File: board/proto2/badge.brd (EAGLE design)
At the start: 136.5 x 119 mm, 59 parts, among them IC1 TLV62569, J1 5051101092

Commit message: reduce LEDs to 14, add tilt switch, draw NFC antenna
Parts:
- removed C19, C23: .1u, rcl:C0201
- removed LED15, LED16: WS2812B, badge:WS2812B
- added S7: SW-200D, badge:SW-200D
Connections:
- removed net N$26: LED15.2, LED16.4
- net +3V3: no longer C19.1, C23.1, LED15.1, LED16.1
- net GND: now also S7.1; no longer C19.2, C23.2, LED15.3, LED16.3
- net N$21: now also S7.2, U1.P37; no longer LED14.2, LED15.4
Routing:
- net ANT: track 0.00 -> 405.1 mm

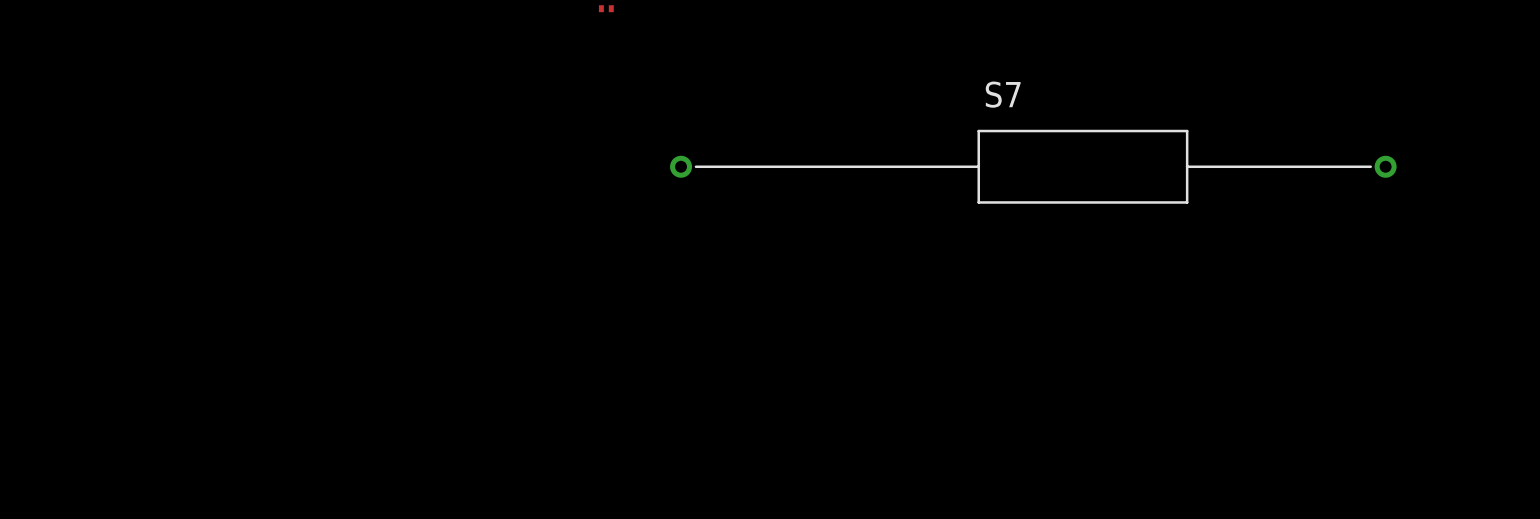
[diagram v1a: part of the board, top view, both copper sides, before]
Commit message: added SD card holder to schematic
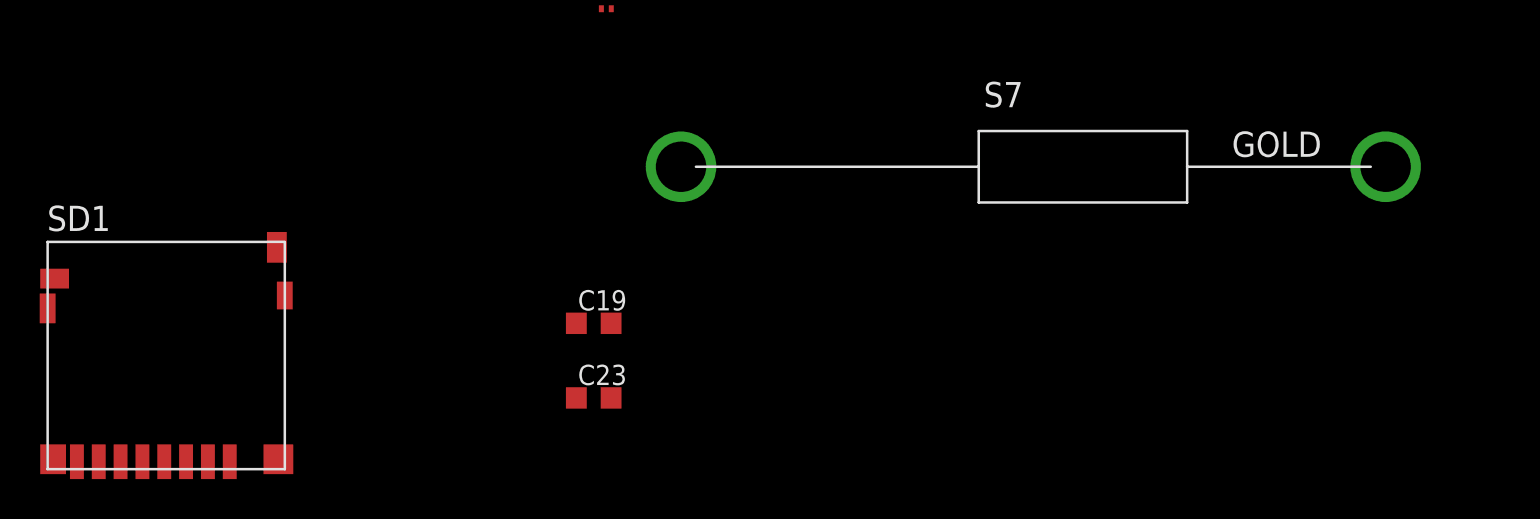
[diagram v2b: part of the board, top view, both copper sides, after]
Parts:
- added C19, C23: 300p, rcl:C0603K
- added SD1: 114-00841-68, badge:114-00841-68
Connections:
- new net ANT: C19.1, C23.1, U1.P25, U1.P26
- new net P0.03: SD1.SWA, U1.P19
- new net P0.04: SD1.7, U1.P20
- new net P0.05: SD1.5, U1.P21
- new net P0.06: SD1.3, U1.P22
- new net P0.07: SD1.2, U1.P23
- net +3V3: now also SD1.4
- net GND: now also C19.2, C23.2, S7.A, SD1.6, SD1.G1, SD1.G2, SD1.G3, SD1.G4, SD1.SWB; no longer S7.1
- net N$21: now also S7.C; no longer S7.2
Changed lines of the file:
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@@
 <layer number="20" name="Dimension" color="15" fill="1" visible="yes" active="yes"/>
 <layer number="21" name="tPlace" color="7" fill="1" visible="yes" active="yes"/>
-<layer number="22" name="bPlace" color="7" fill="1" visible="yes" active="yes"/>
+<layer number="22" name="bPlace" color="7" fill="1" visible="no" active="yes"/>
 <layer number="23" name="tOrigins" color="15" fill="1" visible="yes" active="yes"/>
-<layer number="24" name="bOrigins" color="15" fill="1" visible="yes" active="yes"/>
-<layer number="25" name="tNames" color="7" fill="1" visible="no" active="yes"/>
+<layer number="24" name="bOrigins" color="15" fill="1" visible="no" active="yes"/>
+<layer number="25" name="tNames" color="7" fill="1" visible="yes" active="yes"/>
 <layer number="26" name="bNames" color="7" fill="1" visible="no" active="yes"/>
 <layer number="27" name="tValues" color="7" fill="1" visible="no" active="yes"/>
@@
 <element name="C22" library="rcl" package="C0201" value=".1u" x="-59.69" y="-445.77"/>
 <element name="S7" library="badge" package="SW-200D" value="SW-200D" x="-35.676" y="-453.732"/>
+<element name="C19" library="rcl" package="C0603K" value="300p" x="-60.325" y="-461.6196"/>
+<element name="C23" library="rcl" package="C0603K" value="300p" x="-60.325" y="-465.3788"/>
+<element name="SD1" library="badge" package="114-00841-68" value="114-00841-68" x="-81.8642" y="-469.4682"/>
 </elements>
 <signals>
@@
 <contactref element="C21" pad="2"/>
 <contactref element="C22" pad="2"/>
-<contactref element="S7" pad="1"/>
+<contactref element="S7" pad="A"/>
+<contactref element="C23" pad="2"/>
+<contactref element="C19" pad="2"/>
+<contactref element="SD1" pad="G2"/>
+<contactref element="SD1" pad="G3"/>
+<contactref element="SD1" pad="G1"/>
+<contactref element="SD1" pad="G4"/>
+<contactref element="SD1" pad="6"/>
+<contactref element="SD1" pad="SWB"/>
 <wire x1="-59.44" y1="-440.69" x2="-59.44" y2="-445.77" width="0" layer="19" extent="1-1"/>
 <wire x1="-59.44" y1="-435.61" x2="-59.44" y2="-440.69" width="0" layer="19" extent="1-1"/>
@@
 <wire x1="-59.44" y1="-389.89" x2="-59.44" y2="-394.97" width="0" layer="19" extent="1-1"/>
 <wire x1="-55.926" y1="-453.732" x2="-59.44" y2="-445.77" width="0" layer="19" extent="1-1"/>
+<wire x1="-59.45" y1="-461.6196" x2="-55.926" y2="-453.732" width="0" layer="19" extent="1-1"/>
+<wire x1="-59.45" y1="-465.3788" x2="-59.45" y2="-461.6196" width="0" layer="19" extent="1-1"/>
+<wire x1="-75.8892" y1="-460.2182" x2="-59.45" y2="-461.6196" width="0" layer="19" extent="1-1"/>
+<wire x1="-76.2892" y1="-457.7932" x2="-75.8892" y2="-460.2182" width="0" layer="19" extent="1-1"/>
+<wire x1="-76.2142" y1="-468.4682" x2="-75.8892" y2="-460.2182" width="0" layer="19" extent="1-1"/>
+<wire x1="-84.1642" y1="-468.5932" x2="-76.2142" y2="-468.4682" width="0" layer="19" extent="1-1"/>
+<wire x1="-87.5642" y1="-468.4682" x2="-84.1642" y2="-468.5932" width="0" layer="19" extent="1-1"/>
+<wire x1="-87.8392" y1="-460.8682" x2="-87.5642" y2="-468.4682" width="0" layer="19" extent="1-1"/>
 <wire x1="-57.89" y1="-232.57" x2="-59.44" y2="-389.89" width="0" layer="19" extent="1-1"/>
 <wire x1="-53.09" y1="-229.87" x2="-57.89" y2="-232.57" width="0" layer="19" extent="1-1"/>
@@
 <contactref element="C21" pad="1"/>
 <contactref element="C22" pad="1"/>
+<contactref element="SD1" pad="4"/>
 <wire x1="-55.75" y1="-182.88" x2="-58.84" y2="-191.77" width="0" layer="19" extent="1-1"/>
 <wire x1="-51.8" y1="-185.42" x2="-55.75" y2="-182.88" width="0" layer="19" extent="1-1"/>
@@
 <wire x1="-54.86" y1="-440.69" x2="-59.94" y2="-440.69" width="0" layer="19" extent="1-1"/>
 <wire x1="-54.86" y1="-430.53" x2="-59.94" y2="-430.53" width="0" layer="19" extent="1-1"/>
+<wire x1="-81.9642" y1="-468.5932" x2="-59.94" y2="-445.77" width="0" layer="19" extent="1-1"/>
 <wire x1="56.508846875" y1="21.687634375" x2="-55.75" y2="-182.88" width="0" layer="19" extent="1-1"/>
 <wire x1="51.739375" y1="45.459525" x2="56.508846875" y2="21.687634375" width="0" layer="19" extent="1-1"/>
@@
 </signal>
 <signal name="N$21">
-<contactref element="S7" pad="2"/>
+<contactref element="S7" pad="C"/>
 <contactref element="U1" pad="P37"/>
 <wire x1="70.688115625" y1="92.58431875" x2="-20.426" y2="-453.732" width="0" layer="19" extent="1-1"/>
@@
 <wire x1="85.4202" y1="-43.4594" x2="68.7578" y2="-43.4594" width="0.5334" layer="16"/>
 <wire x1="68.7578" y1="-43.4594" x2="68.7578" y2="-28.8798" width="0.5334" layer="16"/>
+<contactref element="U1" pad="P26"/>
+<contactref element="U1" pad="P25"/>
+<contactref element="C23" pad="1"/>
+<contactref element="C19" pad="1"/>
+<wire x1="67.388115625" y1="88.18431875" x2="67.938115625" y2="89.08431875" width="0" layer="19" extent="1-1"/>
+<wire x1="64.5922" y1="-23.6728" x2="67.388115625" y2="88.18431875" width="0" layer="19" extent="1-16"/>
+<wire x1="-61.2" y1="-461.6196" x2="64.5922" y2="-47.625" width="0" layer="19" extent="1-16"/>
+<wire x1="-61.2" y1="-465.3788" x2="-61.2" y2="-461.6196" width="0" layer="19" extent="1-1"/>
+</signal>
+<signal name="P0.04">
+<contactref element="SD1" pad="7"/>
+<contactref element="U1" pad="P20"/>
+<wire x1="-85.2642" y1="-468.5932" x2="64.638115625" y2="89.08431875" width="0" layer="19" extent="1-1"/>
+</signal>
+<signal name="P0.07">
+<contactref element="SD1" pad="2"/>
+<contactref element="U1" pad="P23"/>
+<wire x1="-79.7642" y1="-468.5932" x2="66.288115625" y2="88.18431875" width="0" layer="19" extent="1-1"/>
+</signal>
+<signal name="P0.06">
+<contactref element="SD1" pad="3"/>
+<contactref element="U1" pad="P22"/>
+<wire x1="-80.8642" y1="-468.5932" x2="65.738115625" y2="89.08431875" width="0" layer="19" extent="1-1"/>
+</signal>
+<signal name="P0.05">
+<contactref element="SD1" pad="5"/>
+<contactref element="U1" pad="P21"/>
+<wire x1="-83.0642" y1="-468.5932" x2="65.188115625" y2="88.18431875" width="0" layer="19" extent="1-1"/>
+</signal>
+<signal name="P0.03">
+<contactref element="SD1" pad="SWA"/>
+<contactref element="U1" pad="P19"/>
+<wire x1="-87.4892" y1="-459.3682" x2="64.088115625" y2="88.18431875" width="0" layer="19" extent="1-1"/>
 </signal>
 </signals>

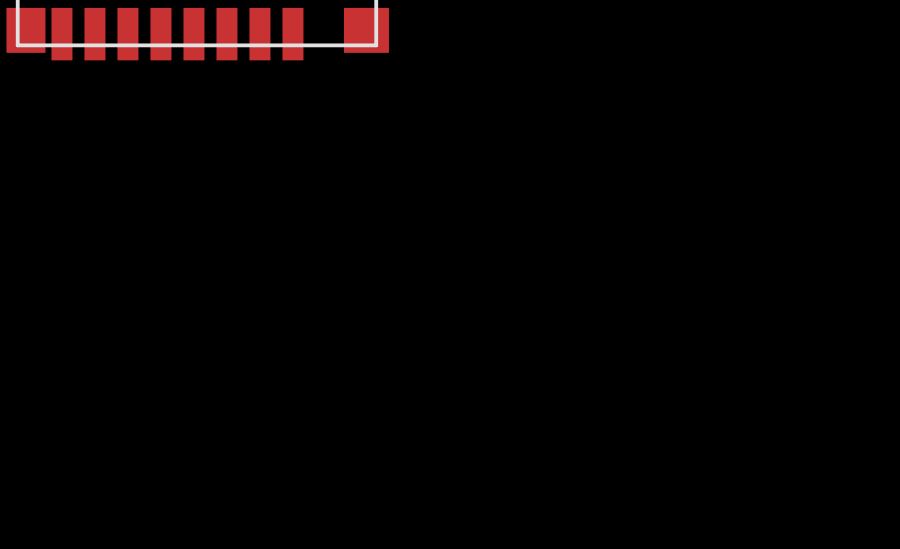
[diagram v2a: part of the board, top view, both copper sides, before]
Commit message: added expansion connector to schematic
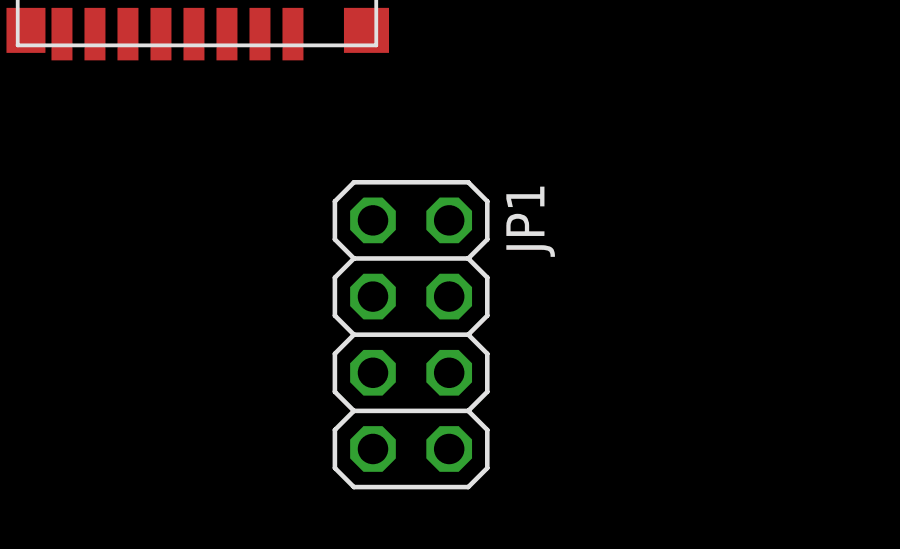
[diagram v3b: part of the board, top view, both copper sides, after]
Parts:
- added JP1: (no value), pinhead:2X04
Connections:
- new net P0.00: JP1.4, U1.P13
- new net P0.01: JP1.6, U1.P14
- new net P0.29: JP1.7, U1.P10
- new net P0.30: JP1.5, U1.P11
- new net P0.31: JP1.3, U1.P12
- net +3V3: now also JP1.1
- net GND: now also JP1.2, JP1.8
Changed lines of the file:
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@@
 <setting verticaltext="up"/>
 </settings>
-<grid distance="1" unitdist="mil" unit="mm" style="lines" multiple="1" display="yes" altdistance="0.012" altunitdist="mm" altunit="mm"/>
+<grid distance="1" unitdist="mil" unit="inch" style="lines" multiple="1" display="yes" altdistance="0.012" altunitdist="mm" altunit="mm"/>
 <layers>
 <layer number="1" name="Top" color="4" fill="1" visible="yes" active="yes"/>
@@
 <element name="C23" library="rcl" package="C0603K" value="300p" x="-60.325" y="-465.3788"/>
 <element name="SD1" library="badge" package="114-00841-68" value="114-00841-68" x="-81.8642" y="-469.4682"/>
+<element name="JP1" library="pinhead" package="2X04" value="" x="-74.7268" y="-478.6122" rot="R270"/>
 </elements>
 <signals>
@@
 <contactref element="SD1" pad="6"/>
 <contactref element="SD1" pad="SWB"/>
+<contactref element="JP1" pad="2"/>
+<contactref element="JP1" pad="8"/>
 <wire x1="-59.44" y1="-440.69" x2="-59.44" y2="-445.77" width="0" layer="19" extent="1-1"/>
 <wire x1="-59.44" y1="-435.61" x2="-59.44" y2="-440.69" width="0" layer="19" extent="1-1"/>
@@
 <wire x1="-76.2892" y1="-457.7932" x2="-75.8892" y2="-460.2182" width="0" layer="19" extent="1-1"/>
 <wire x1="-76.2142" y1="-468.4682" x2="-75.8892" y2="-460.2182" width="0" layer="19" extent="1-1"/>
+<wire x1="-73.4568" y1="-474.8022" x2="-76.2142" y2="-468.4682" width="0" layer="19" extent="1-1"/>
+<wire x1="-73.4568" y1="-482.4222" x2="-73.4568" y2="-474.8022" width="0" layer="19" extent="1-1"/>
 <wire x1="-84.1642" y1="-468.5932" x2="-76.2142" y2="-468.4682" width="0" layer="19" extent="1-1"/>
 <wire x1="-87.5642" y1="-468.4682" x2="-84.1642" y2="-468.5932" width="0" layer="19" extent="1-1"/>
@@
 <contactref element="C22" pad="1"/>
 <contactref element="SD1" pad="4"/>
+<contactref element="JP1" pad="1"/>
 <wire x1="-55.75" y1="-182.88" x2="-58.84" y2="-191.77" width="0" layer="19" extent="1-1"/>
 <wire x1="-51.8" y1="-185.42" x2="-55.75" y2="-182.88" width="0" layer="19" extent="1-1"/>
@@
 <wire x1="-54.86" y1="-430.53" x2="-59.94" y2="-430.53" width="0" layer="19" extent="1-1"/>
 <wire x1="-81.9642" y1="-468.5932" x2="-59.94" y2="-445.77" width="0" layer="19" extent="1-1"/>
+<wire x1="-75.9968" y1="-474.8022" x2="-81.9642" y2="-468.5932" width="0" layer="19" extent="1-1"/>
 <wire x1="56.508846875" y1="21.687634375" x2="-55.75" y2="-182.88" width="0" layer="19" extent="1-1"/>
 <wire x1="51.739375" y1="45.459525" x2="56.508846875" y2="21.687634375" width="0" layer="19" extent="1-1"/>
@@
 <wire x1="-87.4892" y1="-459.3682" x2="64.088115625" y2="88.18431875" width="0" layer="19" extent="1-1"/>
 </signal>
+<signal name="P0.31">
+<contactref element="JP1" pad="3"/>
+<contactref element="U1" pad="P12"/>
+<wire x1="-75.9968" y1="-477.3422" x2="62.788115625" y2="90.93431875" width="0" layer="19" extent="1-1"/>
+</signal>
+<signal name="P0.30">
+<contactref element="JP1" pad="5"/>
+<contactref element="U1" pad="P11"/>
+<wire x1="-75.9968" y1="-479.8822" x2="61.888115625" y2="91.48431875" width="0" layer="19" extent="1-1"/>
+</signal>
+<signal name="P0.29">
+<contactref element="JP1" pad="7"/>
+<contactref element="U1" pad="P10"/>
+<wire x1="-75.9968" y1="-482.4222" x2="62.788115625" y2="92.03431875" width="0" layer="19" extent="1-1"/>
+</signal>
+<signal name="P0.00">
+<contactref element="JP1" pad="4"/>
+<contactref element="U1" pad="P13"/>
+<wire x1="-73.4568" y1="-477.3422" x2="61.888115625" y2="90.38431875" width="0" layer="19" extent="1-1"/>
+</signal>
+<signal name="P0.01">
+<contactref element="JP1" pad="6"/>
+<contactref element="U1" pad="P14"/>
+<wire x1="-73.4568" y1="-479.8822" x2="62.788115625" y2="89.83431875" width="0" layer="19" extent="1-1"/>
+</signal>
 </signals>

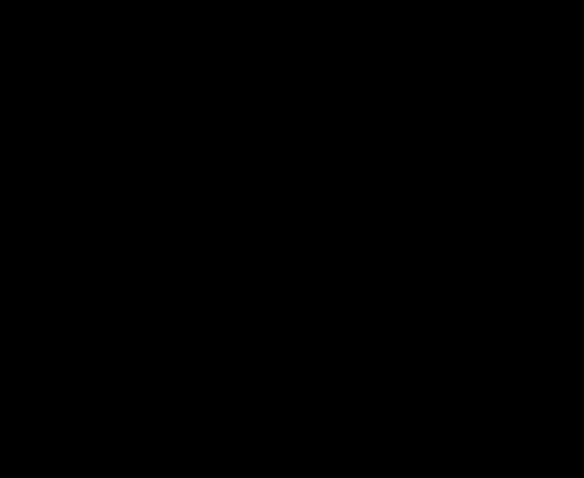
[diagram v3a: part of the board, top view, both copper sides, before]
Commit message: added programming cable connector
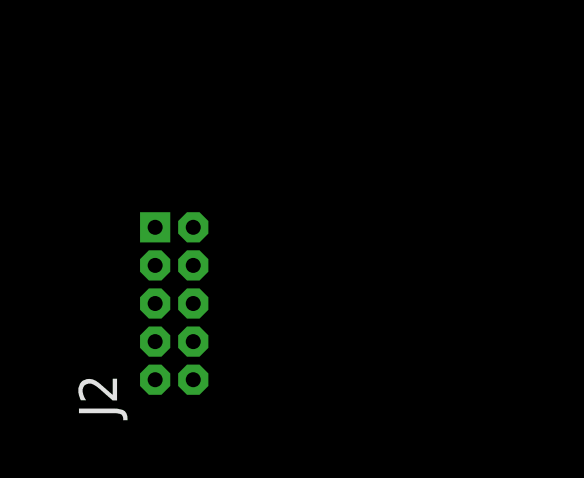
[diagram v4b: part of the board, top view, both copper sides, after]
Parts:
- added J2: M05X2X1.27, badge:2X5X1.27
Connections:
- removed net N$11: C6.1, IC1.1, IC1.4, S6.2
- new net N$26: J2.2, U1.P44
- new net N$31: J2.4, U1.P43
- new net N$32: J2.6, U1.P36
- new net N$33: J2.10, U1.P39
- new net VBAT: C6.1, IC1.1, IC1.4, J2.7, S6.2
- net +3V3: now also J2.1
- net GND: now also J2.3, J2.5
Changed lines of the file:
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@@
 <element name="SD1" library="badge" package="114-00841-68" value="114-00841-68" x="-81.8642" y="-469.4682"/>
 <element name="JP1" library="pinhead" package="2X04" value="" x="-74.7268" y="-478.6122" rot="R270"/>
+<element name="J2" library="badge" package="2X5X1.27" value="M05X2X1.27" x="-96.2406" y="-479.9076"/>
 </elements>
 <signals>
@@
 <contactref element="JP1" pad="2"/>
 <contactref element="JP1" pad="8"/>
+<contactref element="J2" pad="3"/>
+<contactref element="J2" pad="5"/>
 <wire x1="-59.44" y1="-440.69" x2="-59.44" y2="-445.77" width="0" layer="19" extent="1-1"/>
 <wire x1="-59.44" y1="-435.61" x2="-59.44" y2="-440.69" width="0" layer="19" extent="1-1"/>
@@
 <wire x1="-87.5642" y1="-468.4682" x2="-84.1642" y2="-468.5932" width="0" layer="19" extent="1-1"/>
 <wire x1="-87.8392" y1="-460.8682" x2="-87.5642" y2="-468.4682" width="0" layer="19" extent="1-1"/>
+<wire x1="-96.2406" y1="-481.1776" x2="-87.5642" y2="-468.4682" width="0" layer="19" extent="1-1"/>
+<wire x1="-96.2406" y1="-482.4476" x2="-96.2406" y2="-481.1776" width="0" layer="19" extent="1-1"/>
 <wire x1="-57.89" y1="-232.57" x2="-59.44" y2="-389.89" width="0" layer="19" extent="1-1"/>
 <wire x1="-53.09" y1="-229.87" x2="-57.89" y2="-232.57" width="0" layer="19" extent="1-1"/>
@@
 <wire x1="-53.63" y1="-203.99" x2="82.227678125" y2="35.70023125" width="0" layer="19" extent="1-1"/>
 </signal>
-<signal name="N$11">
+<signal name="VBAT">
 <contactref element="IC1" pad="4"/>
 <contactref element="IC1" pad="1"/>
 <contactref element="C6" pad="1"/>
 <contactref element="S6" pad="2"/>
+<contactref element="J2" pad="7"/>
 <wire x1="-51.75" y1="-174.07" x2="-51.8" y2="-179.07" width="0" layer="19" extent="1-1"/>
 <wire x1="-49.85" y1="-171.37" x2="-51.75" y2="-174.07" width="0" layer="19" extent="1-1"/>
 <wire x1="-55.13" y1="-203.99" x2="-51.8" y2="-179.07" width="0" layer="19" extent="1-1"/>
+<wire x1="-96.2406" y1="-483.7176" x2="-55.13" y2="-203.99" width="0" layer="19" extent="1-1"/>
 </signal>
 <signal name="+3V3">
@@
 <contactref element="SD1" pad="4"/>
 <contactref element="JP1" pad="1"/>
+<contactref element="J2" pad="1"/>
 <wire x1="-55.75" y1="-182.88" x2="-58.84" y2="-191.77" width="0" layer="19" extent="1-1"/>
 <wire x1="-51.8" y1="-185.42" x2="-55.75" y2="-182.88" width="0" layer="19" extent="1-1"/>
@@
 <wire x1="-81.9642" y1="-468.5932" x2="-59.94" y2="-445.77" width="0" layer="19" extent="1-1"/>
 <wire x1="-75.9968" y1="-474.8022" x2="-81.9642" y2="-468.5932" width="0" layer="19" extent="1-1"/>
+<wire x1="-96.2406" y1="-479.9076" x2="-81.9642" y2="-468.5932" width="0" layer="19" extent="1-1"/>
 <wire x1="56.508846875" y1="21.687634375" x2="-55.75" y2="-182.88" width="0" layer="19" extent="1-1"/>
 <wire x1="51.739375" y1="45.459525" x2="56.508846875" y2="21.687634375" width="0" layer="19" extent="1-1"/>
@@
 <wire x1="-73.4568" y1="-479.8822" x2="62.788115625" y2="89.83431875" width="0" layer="19" extent="1-1"/>
 </signal>
+<signal name="N$26">
+<contactref element="J2" pad="2"/>
+<contactref element="U1" pad="P44"/>
+<wire x1="-94.9706" y1="-479.9076" x2="69.788115625" y2="96.43431875" width="0" layer="19" extent="1-1"/>
+</signal>
+<signal name="N$31">
+<contactref element="J2" pad="4"/>
+<contactref element="U1" pad="P43"/>
+<wire x1="-94.9706" y1="-481.1776" x2="70.688115625" y2="95.88431875" width="0" layer="19" extent="1-1"/>
+</signal>
+<signal name="N$32">
+<contactref element="J2" pad="6"/>
+<contactref element="U1" pad="P36"/>
+<wire x1="-94.9706" y1="-482.4476" x2="69.788115625" y2="92.03431875" width="0" layer="19" extent="1-1"/>
+</signal>
+<signal name="N$33">
+<contactref element="J2" pad="10"/>
+<contactref element="U1" pad="P39"/>
+<wire x1="-94.9706" y1="-484.9876" x2="70.688115625" y2="93.68431875" width="0" layer="19" extent="1-1"/>
+</signal>
 </signals>

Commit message: add decoupling caps
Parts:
- added C24, C25, C26, C27, C28: .1u, rcl:C0402K
- C1, C10, C11, C12, C13, C14, C15, C16, C17, C18, C2, C20, C21, C22, C3, C4, C5, C8, C9: device rcl:C0201 -> rcl:C0402K
- moved U1 5.82 mm to (61.5, 93.5)
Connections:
- net +3V3: now also C24.1, C25.1, C26.1, C27.1, C28.1
- net GND: now also C24.2, C25.2, C26.2, C27.2, C28.2
